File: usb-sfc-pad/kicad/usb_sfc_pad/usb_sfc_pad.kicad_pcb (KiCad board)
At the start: 2 copper layers, 158.6 x 87.8 mm, 36 parts, among them IC101 PIC16F1459-ISS, J101 532610671, J102 HEADER_6P-2.54, J103 532610271, J104 532610271, J105 532610271, J106 532610271, SW101 SW_Pad, SW102 SW_Pad, SW103 SW_Pad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

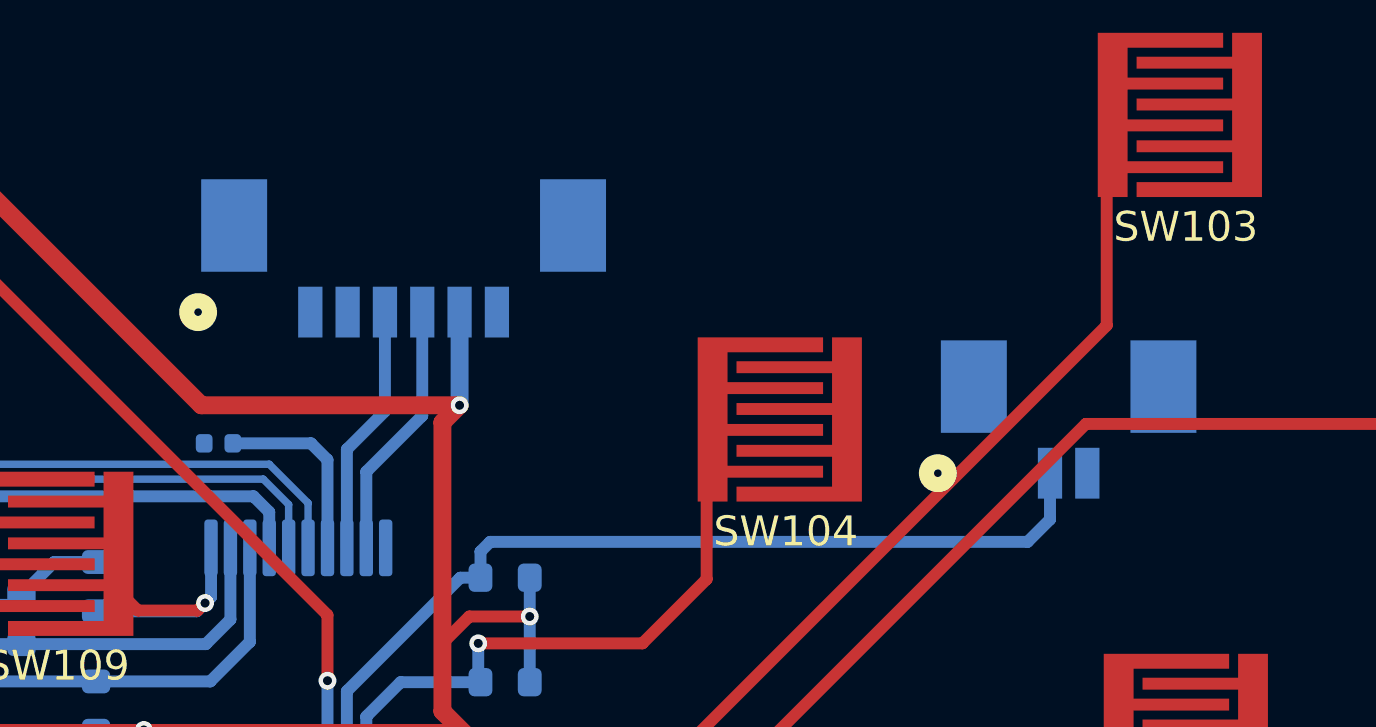
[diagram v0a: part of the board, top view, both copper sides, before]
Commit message: Replace 532610671 with 532610571
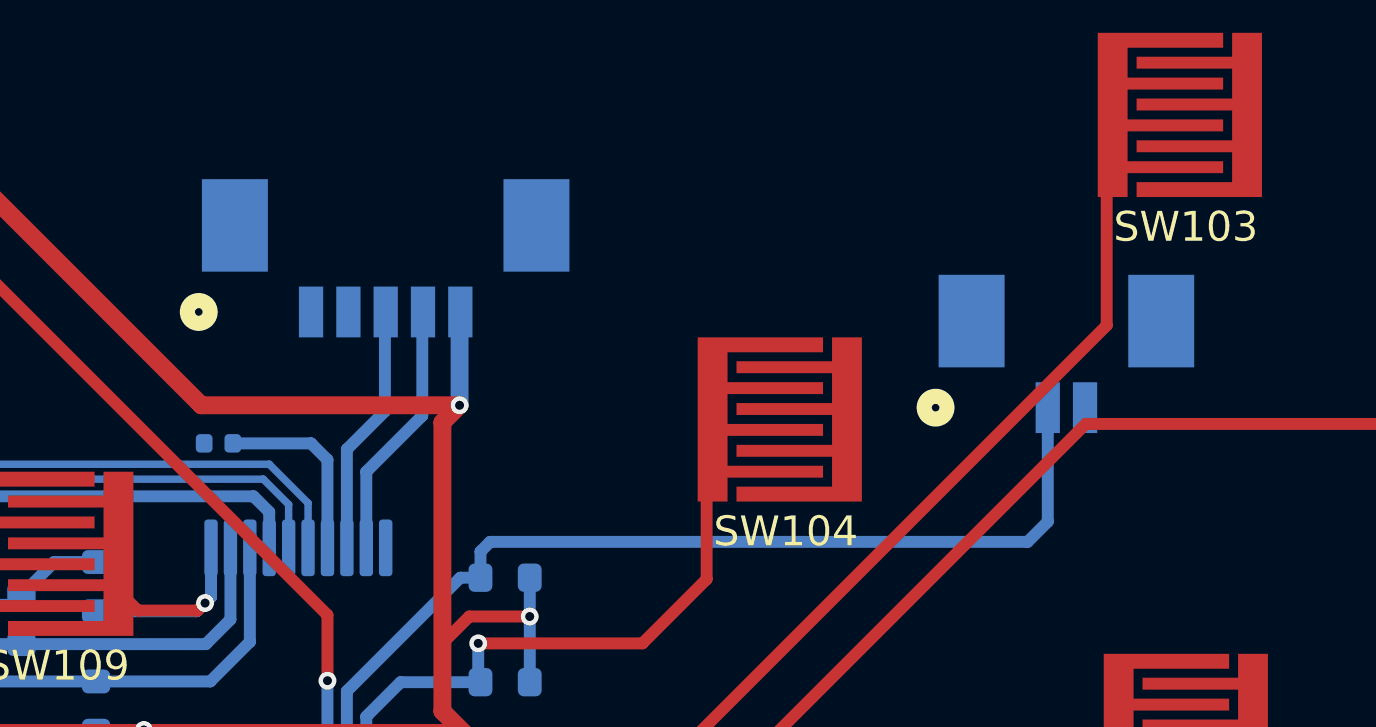
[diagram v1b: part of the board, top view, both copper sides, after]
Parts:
- J101: value 532610671 -> 532610571; footprint Local:CONN_532610001-SD_06_MOL -> Local:CONN_532610001-SD_05_MOL
- moved J103 2.20 mm to (191.1, 104.1)
- moved J101 0.60 mm to (168.3, 100.9)
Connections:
- J101 pad 6: unconnected-(J101-Pad6) -> (no net)
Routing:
- net TR: track 30.2 -> 32.4 mm

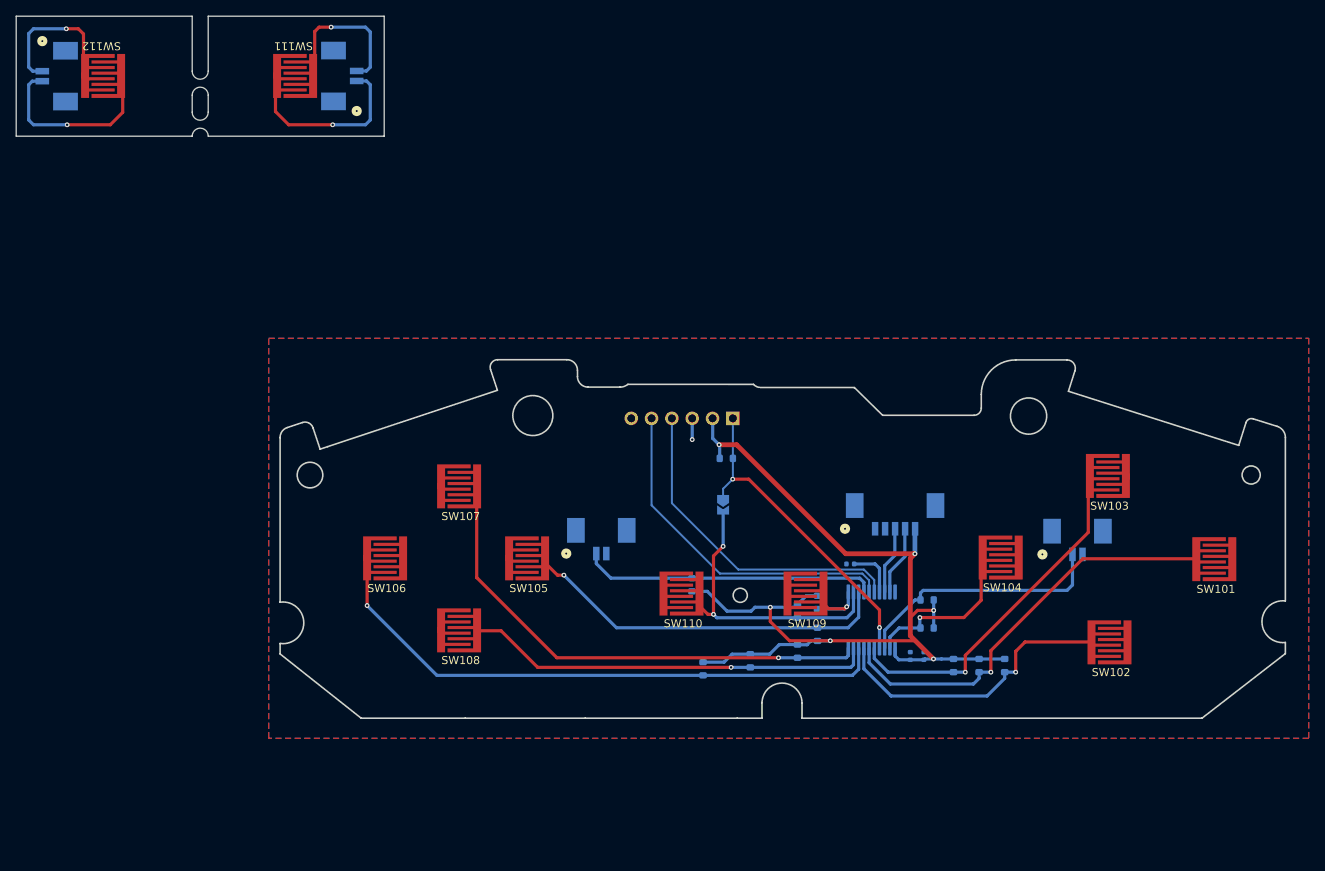
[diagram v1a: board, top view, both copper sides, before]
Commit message: Combine LR board
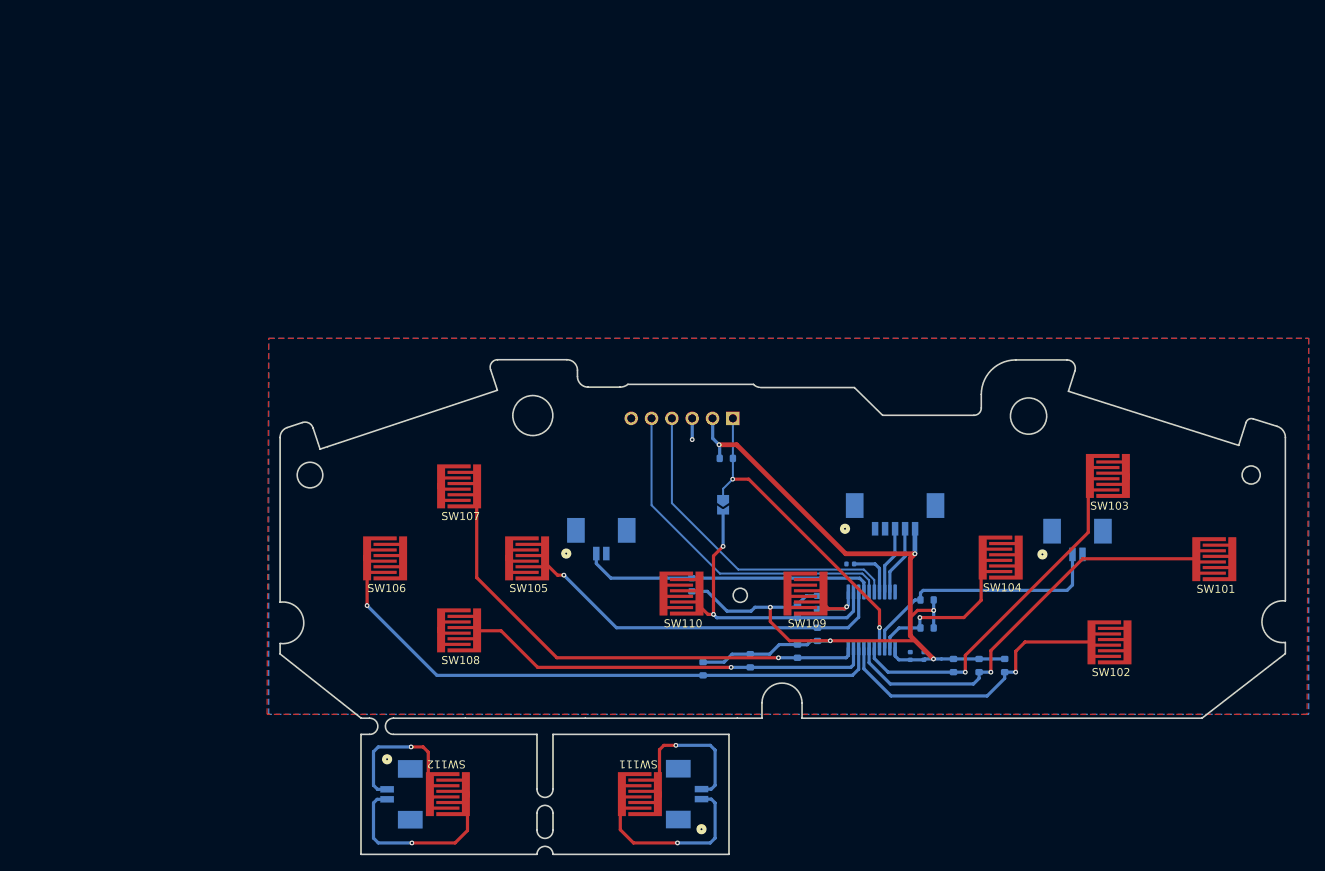
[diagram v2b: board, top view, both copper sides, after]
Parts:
- moved J106 99.6 mm to (107.7, 137.0)
- moved J104 99.6 mm to (141.2, 137.0)
- moved SW111 99.6 mm to (136.4, 137.0)
- moved SW112 99.6 mm to (112.4, 137.0)
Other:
- board size 158.6 x 87.8 mm -> 125.7 x 61.8 mm

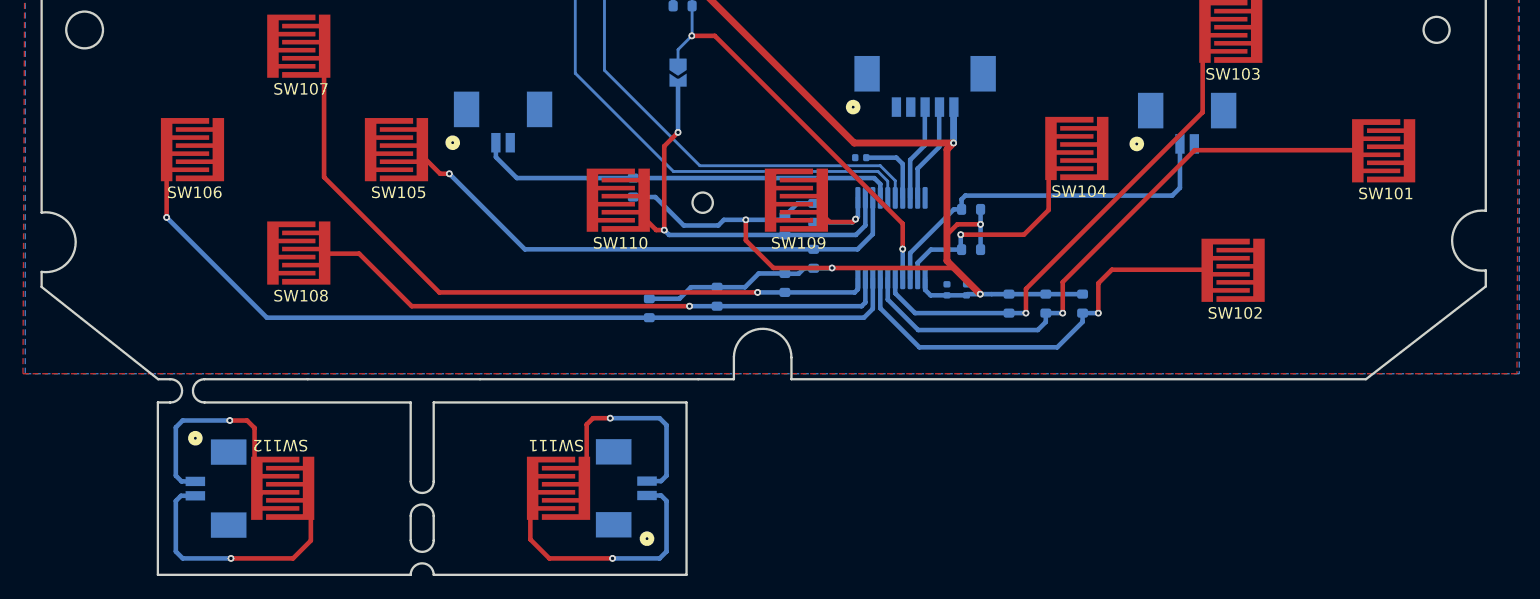
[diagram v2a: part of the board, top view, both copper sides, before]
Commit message: Replace right-angle 2pins with vertical ones
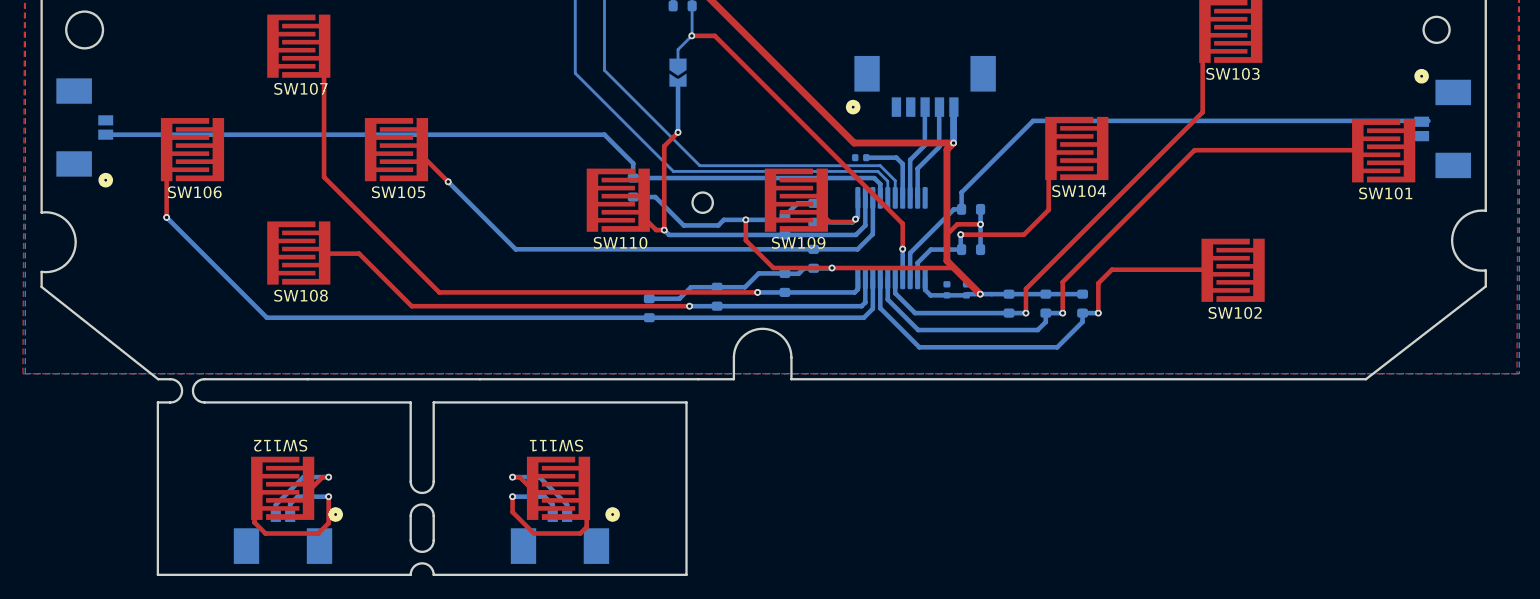
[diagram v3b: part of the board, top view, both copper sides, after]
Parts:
- J103, J104, J105, J106: value 532610271 -> 533980271; footprint Local:CONN_532610001-SD_02_MOL -> Local:CONN02_533980271_MOL
- moved J105 36.6 mm to (95.0, 105.6), turned to -90 degrees
- moved J103 22.5 mm to (213.5, 105.7), turned to 90 degrees
- moved J106 6.35 mm to (112.4, 141.2), turned to 0 degrees
- moved J104 6.33 mm to (136.5, 141.2), turned to 0 degrees
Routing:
- net TL: track 36.9 -> 71.4 mm
- net TR: track 32.4 -> 52.9 mm
- net Net-(J104-Pad1): track 23.8 -> 8.52 mm
- net Net-(J106-Pad2): track 23.5 -> 8.42 mm
- net Net-(J104-Pad2): track 20.2 -> 17.4 mm
- net Net-(J106-Pad1): track 20.0 -> 18.4 mm
